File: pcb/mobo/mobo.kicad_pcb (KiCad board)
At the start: 2 copper layers, 51.6 x 89 mm, 73 parts, among them J1 ISP, J2 PEEL_MOTOR, J3 DRIVE_MOTOR, J4 SW1, J5 SPRING_FINGERS, J6 SW2, J8 USART1, U1 ATmega328PB-A, U2 ATmega328PB-M, U3 LED_RGB, U4 AP1117-50, U5 MC34063AD, U6 SP308xE, U7 DRV8837, U8 DRV8837, Y1 16MHz

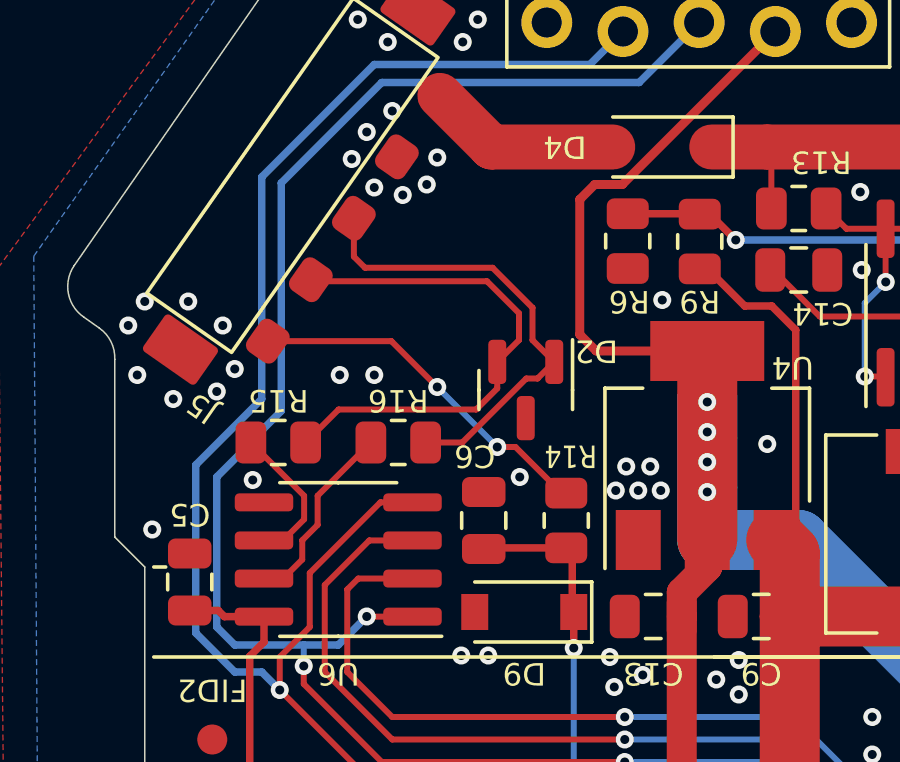
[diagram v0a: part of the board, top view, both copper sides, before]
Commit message: Add X and Y caps to RS485 lines (#19), Update symbols
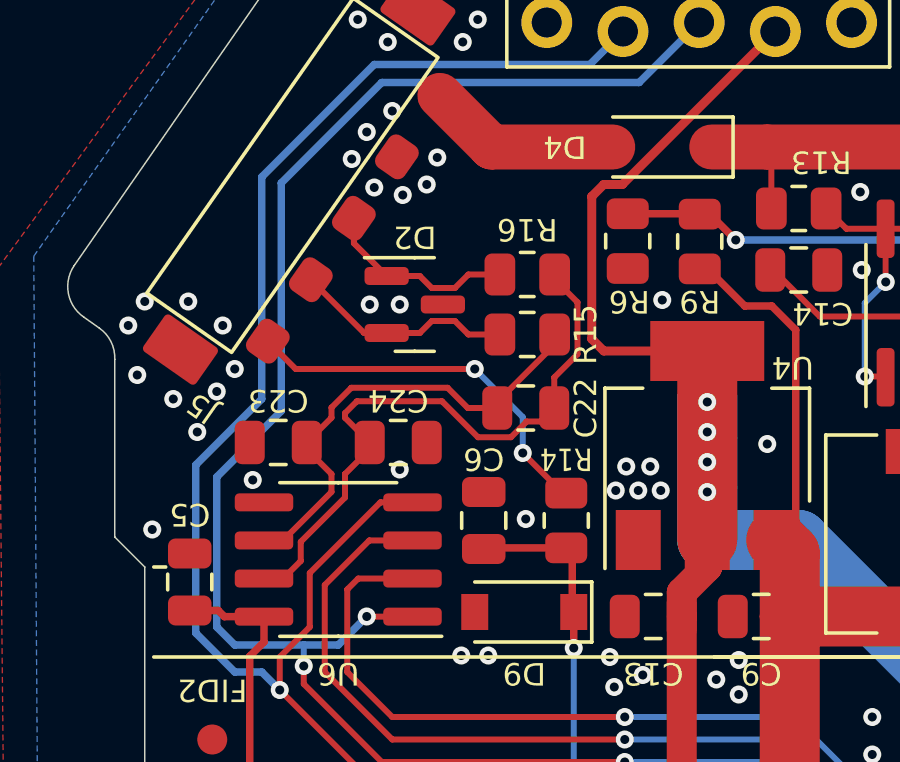
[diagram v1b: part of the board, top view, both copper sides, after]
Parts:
- added C22: 470pF, Capacitor_SMD:C_0805_2012Metric, F.Cu at (115.0, 44.5)
- added C23: 470pF, Capacitor_SMD:C_0805_2012Metric, F.Cu at (106.8, 45.6)
- added C24: 470pF, Capacitor_SMD:C_0805_2012Metric, F.Cu at (110.8, 45.6)
- D9: value MMSZ4689T1G -> MMSZ4684T1G
- moved R15 9.05 mm to (115.0, 42.0), turned to 180 degrees
- moved R16 7.06 mm to (115.0, 40.0), turned to 180 degrees
- moved D2 4.67 mm to (111.3, 41.0), turned to 0 degrees
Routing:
- net /DRV_RS-485-: track 5.75 -> 20.5 mm
- net /DRV_RS-485+: track 4.29 -> 15.7 mm
- net RS-485+: track 17.3 -> 7.39 mm
- net RS-485-: track 15.4 -> 6.50 mm
- net Net-(J5-Pin_5): track 11.9 -> 12.7 mm
- net +5V: track 239.5 -> 238.9 mm
- net GND: vias 118 -> 120

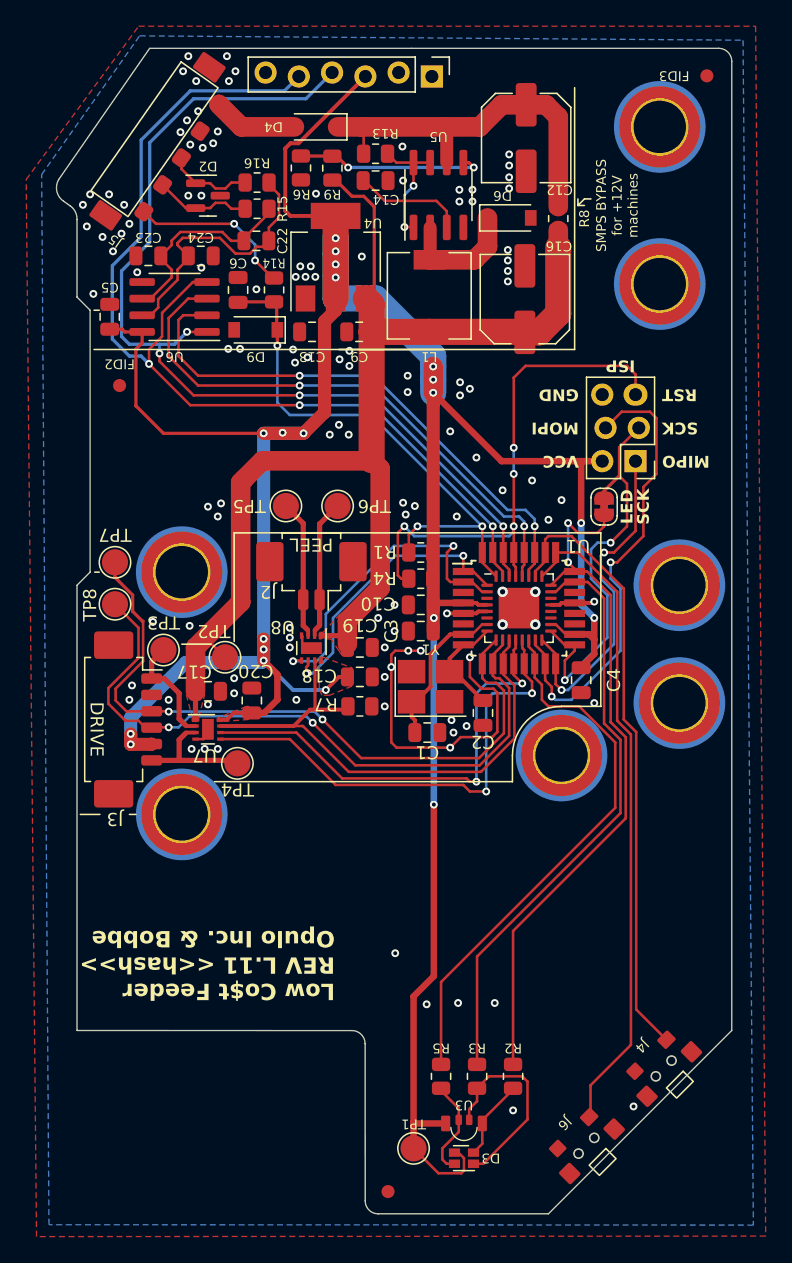
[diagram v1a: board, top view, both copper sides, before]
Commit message: Add push button symbol, Update footprints, Cleanup tracks
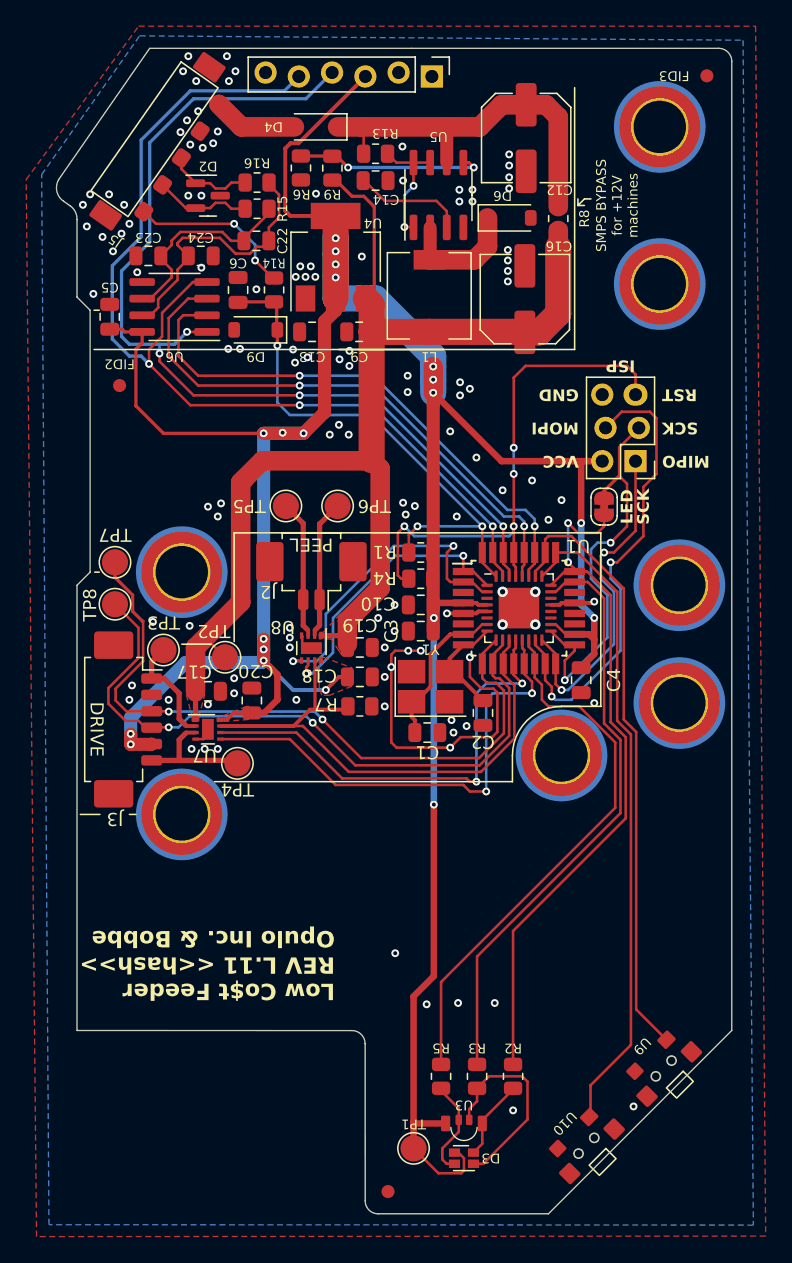
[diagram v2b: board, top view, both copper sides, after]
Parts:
- U10: renamed from J6; value SW2 -> ~
- U9: renamed from J4; value SW1 -> ~
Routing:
- net /DRV_RS-485+: track 15.7 -> 14.3 mm
- net /DRV_RS-485-: track 20.5 -> 19.7 mm
